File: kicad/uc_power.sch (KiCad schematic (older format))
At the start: 36 parts, among them U1_? TMS320F28388DZWTS

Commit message: remove isolation GPIO's and replace it by free pins at IGBT
I remove completely the isolated inputs pins cause I've 8 pins free at
IGBT isolated interfase, so I leave 4 for outpus and 4 for inputs with
one isolated stage, the same as the previous isolated GPIO sheet..
I've improved the DBG sheet and some other details,. I'm ready to make
some electrical checks and fchoose the parts codes and footprints.. go
for it!
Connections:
- net labels added: 1V2C, 1V2uC, 3V3uC
- net labels removed: 1V2, GNDA, IN_1V2C, IN_3V3C, TMS320F28388DZWTS
- wire segments 263 -> 258
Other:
- note added: "DECOUPLING FILTERS"
- moved on the sheet: C?, L?, U1_?D, U1_?E

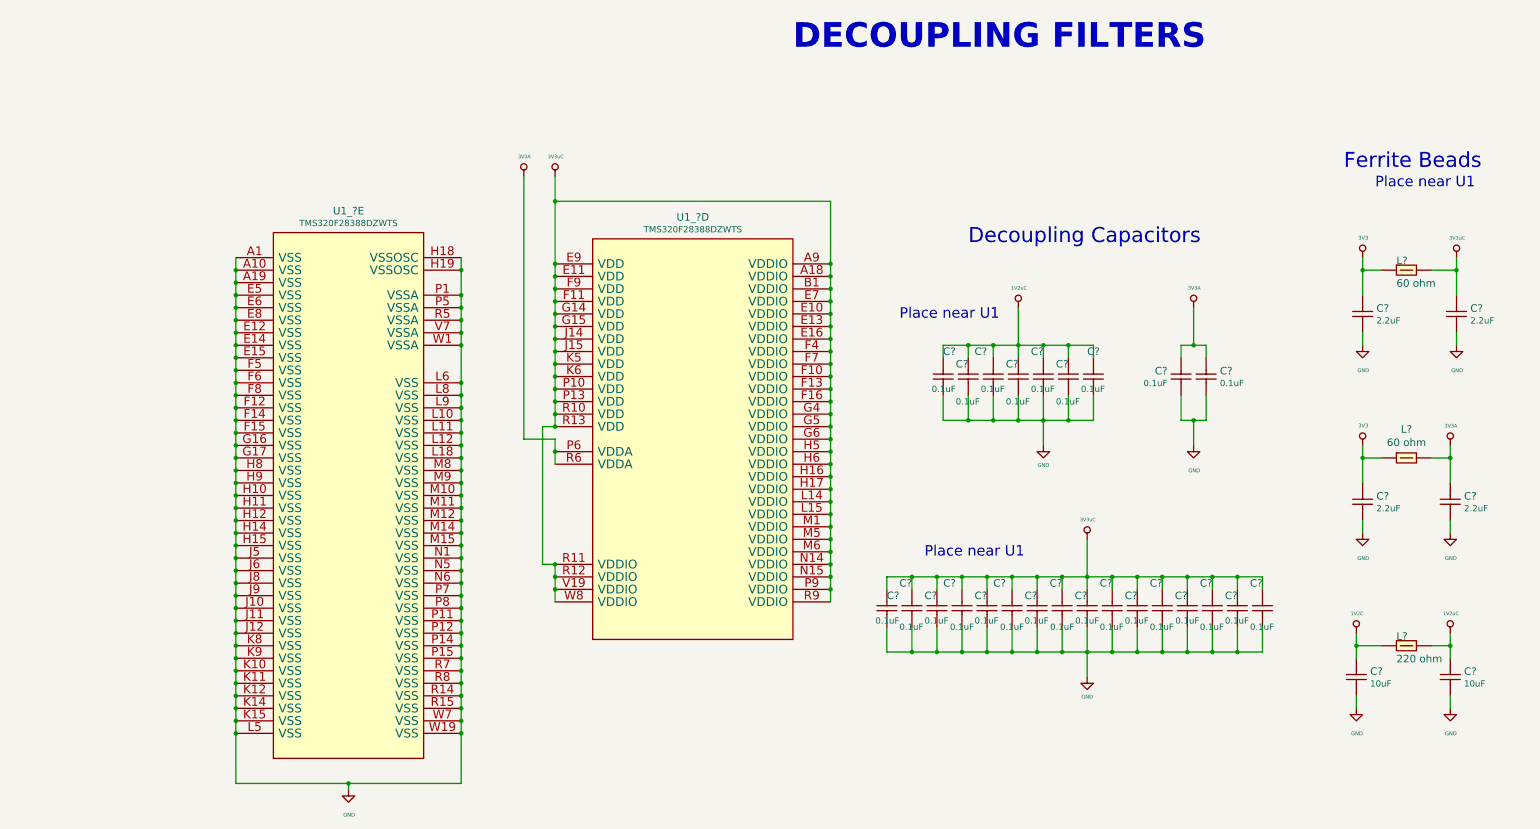
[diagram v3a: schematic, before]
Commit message: added 4 push buttons and more gpios on LCD connector
just to have more UI options. With those I'd manage graphics LCD plus 4
buttons, and charaveter LCD. or the embedded EVE graphic LCD
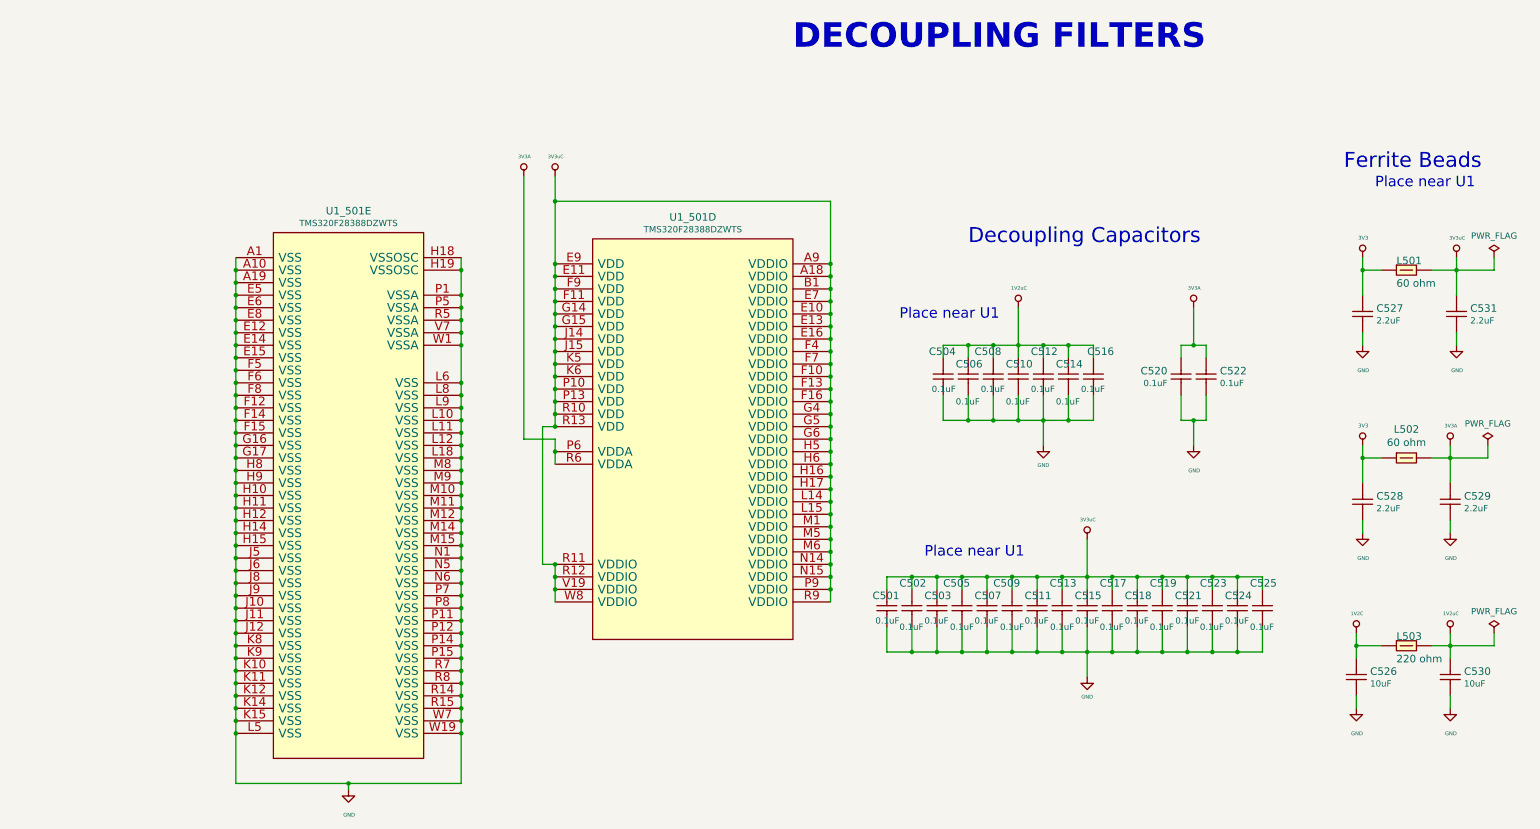
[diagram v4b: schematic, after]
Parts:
- gave numbers to parts that had none: 35

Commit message: begin PCB!! it's amess but IT IS
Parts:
- C501, C502, C503, C504, C505, C506, C507, C508, C509, C510, C511, C512, C513, C514, C515, C516, C517, C518, C519, C520, C521, C522, C523, C524, C525, C526, C527, C528, C529, C530, C531: footprint (none) -> Capacitor_SMD:C_0603_1608Metric
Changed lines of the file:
@@
 F 0 "C501" V 8000 5600 60  0000 L CNN
 F 1 "0.1uF" V 7800 5600 50  0000 L CNN
-F 2 "" H 7850 5700 50  0001 C CNN
+F 2 "Capacitor_SMD:C_0603_1608Metric" H 7850 5700 50  0001 C CNN
 F 3 "" H 7850 5700 50  0001 C CNN
 F 4 "0.1uF" V 2050 -1200 60  0001 C CNN "ValueDisplayed"
@@
 F 0 "C502" V 8300 5800 60  0000 R CNN
 F 1 "0.1uF" V 7950 5800 50  0000 R CNN
-F 2 "" H 8050 5700 50  0001 C CNN
+F 2 "Capacitor_SMD:C_0603_1608Metric" H 8050 5700 50  0001 C CNN
 F 3 "" H 8050 5700 50  0001 C CNN
 F 4 "0.1uF" V 2050 -1200 60  0001 C CNN "ValueDisplayed"
@@
 F 0 "C503" V 8400 5800 60  0000 R CNN
 F 1 "0.1uF" V 8200 5800 50  0000 R CNN
-F 2 "" H 8250 5700 50  0001 C CNN
+F 2 "Capacitor_SMD:C_0603_1608Metric" H 8250 5700 50  0001 C CNN
 F 3 "" H 8250 5700 50  0001 C CNN
 F 4 "0.1uF" V 2050 -1200 60  0001 C CNN "ValueDisplayed"
@@
 F 0 "C505" V 8700 5850 60  0000 R CNN
 F 1 "0.1uF" V 8350 5700 50  0000 C CNN
-F 2 "" H 8450 5700 50  0001 C CNN
+F 2 "Capacitor_SMD:C_0603_1608Metric" H 8450 5700 50  0001 C CNN
 F 3 "" H 8450 5700 50  0001 C CNN
 F 4 "0.1uF" V 2050 -1200 60  0001 C CNN "ValueDisplayed"
@@
 F 0 "C507" V 8800 5800 60  0000 R CNN
 F 1 "0.1uF" V 8600 5800 50  0000 R CNN
-F 2 "" H 8650 5700 50  0001 C CNN
+F 2 "Capacitor_SMD:C_0603_1608Metric" H 8650 5700 50  0001 C CNN
 F 3 "" H 8650 5700 50  0001 C CNN
 F 4 "0.1uF" V 2050 -1200 60  0001 C CNN "ValueDisplayed"
@@
 F 0 "C509" V 9100 5850 60  0000 R CNN
 F 1 "0.1uF" V 8750 5700 50  0000 C CNN
-F 2 "" H 8850 5700 50  0001 C CNN
+F 2 "Capacitor_SMD:C_0603_1608Metric" H 8850 5700 50  0001 C CNN
 F 3 "" H 8850 5700 50  0001 C CNN
 F 4 "0.1uF" V 2050 -1200 60  0001 C CNN "ValueDisplayed"
@@
 F 0 "C511" V 9200 5800 60  0000 R CNN
 F 1 "0.1uF" V 9000 5800 50  0000 R CNN
-F 2 "" H 9050 5700 50  0001 C CNN
+F 2 "Capacitor_SMD:C_0603_1608Metric" H 9050 5700 50  0001 C CNN
 F 3 "" H 9050 5700 50  0001 C CNN
 F 4 "0.1uF" V 2050 -1200 60  0001 C CNN "ValueDisplayed"
@@
 F 0 "C513" V 9500 5800 60  0000 R CNN
 F 1 "0.1uF" V 9150 5700 50  0000 C CNN
-F 2 "" H 9250 5700 50  0001 C CNN
+F 2 "Capacitor_SMD:C_0603_1608Metric" H 9250 5700 50  0001 C CNN
 F 3 "" H 9250 5700 50  0001 C CNN
 F 4 "0.1uF" V 2050 -1200 60  0001 C CNN "ValueDisplayed"
@@
 F 0 "C515" V 9600 5800 60  0000 R CNN
 F 1 "0.1uF" V 9400 5700 50  0000 C CNN
-F 2 "" H 9450 5700 50  0001 C CNN
+F 2 "Capacitor_SMD:C_0603_1608Metric" H 9450 5700 50  0001 C CNN
 F 3 "" H 9450 5700 50  0001 C CNN
 F 4 "0.1uF" V 2050 -1200 60  0001 C CNN "ValueDisplayed"
@@
 F 0 "C517" V 9900 5800 60  0000 R CNN
 F 1 "0.1uF" V 9550 5800 50  0000 R CNN
-F 2 "" H 9650 5700 50  0001 C CNN
+F 2 "Capacitor_SMD:C_0603_1608Metric" H 9650 5700 50  0001 C CNN
 F 3 "" H 9650 5700 50  0001 C CNN
 F 4 "0.1uF" V 2050 -1200 60  0001 C CNN "ValueDisplayed"
@@
 F 0 "C518" V 10000 5800 60  0000 R CNN
 F 1 "0.1uF" V 9800 5800 50  0000 R CNN
-F 2 "" H 9850 5700 50  0001 C CNN
+F 2 "Capacitor_SMD:C_0603_1608Metric" H 9850 5700 50  0001 C CNN
 F 3 "" H 9850 5700 50  0001 C CNN
 F 4 "0.1uF" V 2050 -1200 60  0001 C CNN "ValueDisplayed"
@@
 F 0 "C519" V 10300 5800 60  0000 R CNN
 F 1 "0.1uF" V 9950 5800 50  0000 R CNN
-F 2 "" H 10050 5700 50  0001 C CNN
+F 2 "Capacitor_SMD:C_0603_1608Metric" H 10050 5700 50  0001 C CNN
 F 3 "" H 10050 5700 50  0001 C CNN
 F 4 "0.1uF" V 2050 -1200 60  0001 C CNN "ValueDisplayed"
@@
 F 0 "C521" V 10400 5800 60  0000 R CNN
 F 1 "0.1uF" V 10200 5700 50  0000 C CNN
-F 2 "" H 10250 5700 50  0001 C CNN
+F 2 "Capacitor_SMD:C_0603_1608Metric" H 10250 5700 50  0001 C CNN
 F 3 "" H 10250 5700 50  0001 C CNN
 F 4 "0.1uF" V 2050 -1200 60  0001 C CNN "ValueDisplayed"
@@
 F 0 "C523" V 10700 5800 60  0000 R CNN
 F 1 "0.1uF" V 10350 5800 50  0000 R CNN
-F 2 "" H 10450 5700 50  0001 C CNN
+F 2 "Capacitor_SMD:C_0603_1608Metric" H 10450 5700 50  0001 C CNN
 F 3 "" H 10450 5700 50  0001 C CNN
 F 4 "0.1uF" V 2050 -1200 60  0001 C CNN "ValueDisplayed"
@@
 F 0 "C524" V 10800 5800 60  0000 R CNN
 F 1 "0.1uF" V 10600 5800 50  0000 R CNN
-F 2 "" H 10650 5700 50  0001 C CNN
+F 2 "Capacitor_SMD:C_0603_1608Metric" H 10650 5700 50  0001 C CNN
 F 3 "" H 10650 5700 50  0001 C CNN
 F 4 "0.1uF" V 2050 -1200 60  0001 C CNN "ValueDisplayed"
@@
 F 0 "C525" V 11100 5800 60  0000 R CNN
 F 1 "0.1uF" V 10750 5800 50  0000 R CNN
-F 2 "" H 10850 5700 50  0001 C CNN
+F 2 "Capacitor_SMD:C_0603_1608Metric" H 10850 5700 50  0001 C CNN
 F 3 "" H 10850 5700 50  0001 C CNN
 F 4 "0.1uF" V 2050 -1200 60  0001 C CNN "ValueDisplayed"
@@
 F 0 "C508" V 8950 4000 60  0000 R CNN
 F 1 "0.1uF" V 8650 3950 50  0000 R CNN
-F 2 "" H 8700 3850 50  0001 C CNN
+F 2 "Capacitor_SMD:C_0603_1608Metric" H 8700 3850 50  0001 C CNN
 F 3 "" H 8700 3850 50  0001 C CNN
 F 4 "0.1uF" V 2200 -950 60  0001 C CNN "ValueDisplayed"
@@
 F 0 "C510" V 9050 3950 60  0000 R CNN
 F 1 "0.1uF" V 8750 3950 50  0000 R CNN
-F 2 "" H 8900 3850 50  0001 C CNN
+F 2 "Capacitor_SMD:C_0603_1608Metric" H 8900 3850 50  0001 C CNN
 F 3 "" H 8900 3850 50  0001 C CNN
 F 4 "0.1uF" V 2200 -950 60  0001 C CNN "ValueDisplayed"
@@
 F 0 "C512" V 9350 3950 60  0000 R CNN
 F 1 "0.1uF" V 9050 3950 50  0000 R CNN
-F 2 "" H 9100 3850 50  0001 C CNN
+F 2 "Capacitor_SMD:C_0603_1608Metric" H 9100 3850 50  0001 C CNN
 F 3 "" H 9100 3850 50  0001 C CNN
 F 4 "0.1uF" V 2200 -950 60  0001 C CNN "ValueDisplayed"
@@
 F 0 "C514" V 9450 3950 60  0000 R CNN
 F 1 "0.1uF" V 9150 3950 50  0000 R CNN
-F 2 "" H 9300 3850 50  0001 C CNN
+F 2 "Capacitor_SMD:C_0603_1608Metric" H 9300 3850 50  0001 C CNN
 F 3 "" H 9300 3850 50  0001 C CNN
 F 4 "0.1uF" V 2200 -950 60  0001 C CNN "ValueDisplayed"
@@
 F 0 "C516" V 9750 3900 60  0000 R CNN
 F 1 "0.1uF" V 9450 3950 50  0000 R CNN
-F 2 "" H 9500 3850 50  0001 C CNN
+F 2 "Capacitor_SMD:C_0603_1608Metric" H 9500 3850 50  0001 C CNN
 F 3 "" H 9500 3850 50  0001 C CNN
 F 4 "0.1uF" V 2200 -950 60  0001 C CNN "ValueDisplayed"
@@
 F 0 "C520" V 10295 3959 60  0000 L CNN
 F 1 "0.1uF" V 10197 3959 50  0000 L CNN
-F 2 "" H 10200 3850 50  0001 C CNN
+F 2 "Capacitor_SMD:C_0603_1608Metric" H 10200 3850 50  0001 C CNN
 F 3 "" H 10200 3850 50  0001 C CNN
 F 4 "0.1uF" V 2200 -950 60  0001 C CNN "ValueDisplayed"
@@
 F 0 "C522" V 10495 3740 60  0000 R CNN
 F 1 "0.1uF" V 10397 3740 50  0000 R CNN
-F 2 "" H 10400 3850 50  0001 C CNN
+F 2 "Capacitor_SMD:C_0603_1608Metric" H 10400 3850 50  0001 C CNN
 F 3 "" H 10400 3850 50  0001 C CNN
 F 4 "0.1uF" V 2200 -950 60  0001 C CNN "ValueDisplayed"
@@
 F 0 "C504" V 8550 3750 60  0000 L CNN
 F 1 "0.1uF" V 8250 3750 50  0000 L CNN
-F 2 "" H 8300 3850 50  0001 C CNN
+F 2 "Capacitor_SMD:C_0603_1608Metric" H 8300 3850 50  0001 C CNN
 F 3 "" H 8300 3850 50  0001 C CNN
 F 4 "0.1uF" V 2200 -950 60  0001 C CNN "ValueDisplayed"
@@
 F 0 "C506" V 8650 3950 60  0000 R CNN
 F 1 "0.1uF" V 8350 3950 50  0000 R CNN
-F 2 "" H 8500 3850 50  0001 C CNN
+F 2 "Capacitor_SMD:C_0603_1608Metric" H 8500 3850 50  0001 C CNN
 F 3 "" H 8500 3850 50  0001 C CNN
 F 4 "0.1uF" V 2200 -950 60  0001 C CNN "ValueDisplayed"
@@
 F 0 "C530" V 12445 6140 60  0000 R CNN
 F 1 "10uF" V 12347 6140 50  0000 R CNN
-F 2 "" H 12350 6250 50  0001 C CNN
+F 2 "Capacitor_SMD:C_0603_1608Metric" H 12350 6250 50  0001 C CNN
 F 3 "" H 12350 6250 50  0001 C CNN
 F 4 "10uF" V -1350 -950 60  0001 C CNN "ValueDisplayed"
@@
 F 0 "C531" V 12405 3360 60  0000 L CNN
 F 1 "2.2uF" V 12503 3360 50  0000 L CNN
-F 2 "" H 12400 3250 50  0001 C CNN
+F 2 "Capacitor_SMD:C_0603_1608Metric" H 12400 3250 50  0001 C CNN
 F 3 "" H 12400 3250 50  0001 C CNN
 F 4 "2.2uF" V -1300 -950 60  0001 C CNN "ValueDisplayed"
@@
 F 0 "C529" V 12355 4860 60  0000 L CNN
 F 1 "2.2uF" V 12453 4860 50  0000 L CNN
-F 2 "" H 12350 4750 50  0001 C CNN
+F 2 "Capacitor_SMD:C_0603_1608Metric" H 12350 4750 50  0001 C CNN
 F 3 "" H 12350 4750 50  0001 C CNN
 F 4 "2.2uF" V -1350 -950 60  0001 C CNN "ValueDisplayed"
@@
 F 0 "C528" V 11655 4860 60  0000 L CNN
 F 1 "2.2uF" V 11753 4860 50  0000 L CNN
-F 2 "" H 11650 4750 50  0001 C CNN
+F 2 "Capacitor_SMD:C_0603_1608Metric" H 11650 4750 50  0001 C CNN
 F 3 "" H 11650 4750 50  0001 C CNN
 F 4 "2.2uF" V -850 -950 60  0001 C CNN "ValueDisplayed"
@@
 F 0 "C527" V 11655 3360 60  0000 L CNN
 F 1 "2.2uF" V 11753 3360 50  0000 L CNN
-F 2 "" H 11650 3250 50  0001 C CNN
+F 2 "Capacitor_SMD:C_0603_1608Metric" H 11650 3250 50  0001 C CNN
 F 3 "" H 11650 3250 50  0001 C CNN
 F 4 "2.2uF" V -850 -950 60  0001 C CNN "ValueDisplayed"
@@
 F 0 "C526" V 11605 6260 60  0000 L CNN
 F 1 "10uF" V 11703 6260 50  0000 L CNN
-F 2 "" H 11600 6150 50  0001 C CNN
+F 2 "Capacitor_SMD:C_0603_1608Metric" H 11600 6150 50  0001 C CNN
 F 3 "" H 11600 6150 50  0001 C CNN
 F 4 "10uF" V -900 -950 60  0001 C CNN "ValueDisplayed"

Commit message: I've passed all footprin to layout BUT...
I've passed all, first glance... I need to confirm in details a lot of
things. The objetive for these is to have an aproximation of the size
I'll need to make the board.. then I choose the final detailed footprint
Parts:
- C501, C502, C503, C504, C505, C506, C507, C508, C509, C510, C511, C512, C513, C514, C515, C516, C517, C518, C519, C520, C521, C522, C523, C524, C525, C526, C527, C528, C529, C530, C531: footprint Capacitor_SMD:C_0603_1608Metric -> servo:C_0603_1608Metric
- L501, L502, L503: footprint (none) -> Inductor_SMD:L_0603_1608Metric
- U1_501: footprint (none) -> servo:BGA337CP80_19X19_1600X1600X140B50N

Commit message: passed all footprint, preliminarly.. and taken a pic
I've passed all 3d models, and make a pic of that, it's the first
impresion, but it need's more indeed reviews
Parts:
- renumbered U1_501 to U301
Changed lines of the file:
@@
 $EndComp
 $Comp
-L servo:TMS320F28388 U1_501
+L servo:TMS320F28388 U301
 U 4 1 5DB38F9F
 P 6300 4300
-F 0 "U1_501" H 6300 6073 60  0000 C CNN
+F 0 "U301" H 6300 6073 60  0000 C CNN
 F 1 "TMS320F28388DZWTS" H 6300 5975 50  0000 C CNN
 F 2 "servo:BGA337CP80_19X19_1600X1600X140B50N" H 6300 4300 50  0001 C CNN
@@
 Connection ~ 2650 2950
 $Comp
-L servo:TMS320F28388 U1_501
+L servo:TMS320F28388 U301
 U 5 1 5DB38FA0
 P 3550 4750
-F 0 "U1_501" H 3550 7023 60  0000 C CNN
+F 0 "U301" H 3550 7023 60  0000 C CNN
 F 1 "TMS320F28388DZWTS" H 3550 6925 50  0000 C CNN
 F 2 "servo:BGA337CP80_19X19_1600X1600X140B50N" H 3550 4750 50  0001 C CNN
